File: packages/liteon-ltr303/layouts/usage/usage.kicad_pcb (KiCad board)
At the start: 2 copper layers, 5 parts

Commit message: fix checksum
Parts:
- R2, R3: value 10kΩ ±1% 62.5mW -> 4.7kΩ ±1% 62.5mW; footprint UNI_ROYAL_0402WGF1002TCE:R0402 -> UNI_ROYAL_0402WGF4701TCE:R0402
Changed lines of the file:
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@@
             )
         )
-        (property "checksum" "51bbabab493bf5d6f2e8ff7587227a5311f24aee7123d9f581721a4bd211b3f4"
+        (property "checksum" "ab8092c5206f4459d5858c652ec7d6e0be05596abb3bee276846f4a8302a4aa7"
             (at 0 0 0)
             (layer "User.9")
@@
             )
         )
-        (property "__atopile_lib_fp_hash__" "f4224e4a-fd5d-eb39-1573-fab7e7d24610"
+        (property "__atopile_lib_fp_hash__" "30b3a641-de78-5481-970c-0779282f0079"
             (at 0 0 0)
             (layer "User.9")
@@
         )
     )
-    (footprint "UNI_ROYAL_0402WGF1002TCE:R0402"
+    (footprint "UNI_ROYAL_0402WGF4701TCE:R0402"
         (layer "F.Cu")
         (at 0 -30 0)
@@
             )
         )
-        (property "Value" "10kΩ ±1% 62.5mW"
+        (property "Value" "4.7kΩ ±1% 62.5mW"
             (at 0 4 0)
             (layer "F.Fab")
@@
             )
         )
-        (property "checksum" "51bbabab493bf5d6f2e8ff7587227a5311f24aee7123d9f581721a4bd211b3f4"
+        (property "checksum" "0d598954a8da2c09676a6e60c961071badf97dacbdec513c849e6b4b9da6a890"
             (at 0 0 0)
             (layer "User.9")
@@
             )
         )
-        (property "__atopile_lib_fp_hash__" "f4224e4a-fd5d-eb39-1573-fab7e7d24610"
-            (at 0 0 0)
-            (layer "User.9")
-            (hide yes)
-            (effects
-                (font
-                    (size 0.125 0.125)
-                    (thickness 0.01875)
-                )
-            )
-        )
-        (property "LCSC" "C25744"
+        (property "__atopile_lib_fp_hash__" "78e51c6c-4851-23a9-a200-a953cf32da8a"
+            (at 0 0 0)
+            (layer "User.9")
+            (hide yes)
+            (effects
+                (font
+                    (size 0.125 0.125)
+                    (thickness 0.01875)
+                )
+            )
+        )
+        (property "LCSC" "C25900"
             (at 0 0 0)
             (layer "User.9")
@@
             )
         )
-        (property "Partnumber" "0402WGF1002TCE"
+        (property "Partnumber" "0402WGF4701TCE"
             (at 0 0 0)
             (layer "User.9")
@@
             )
         )
-        (property "PARAM_resistance" "{\"type\": \"Quantity_Interval_Disjoint\", \"data\": {\"intervals\": {\"type\": \"Numeric_Interval_Disjoint\", \"data\": {\"intervals\": [{\"type\": \"Numeric_Interval\", \"data\": {\"min\": 9900.000002235174, \"max\": 10099.999997764826}}]}}, \"unit\": \"ohm\"}}"
-            (at 0 0 0)
-            (layer "User.9")
-            (hide yes)
-            (effects
-                (font
-                    (size 0.125 0.125)
-                    (thickness 0.01875)
-                )
-            )
-        )
-        (property "Datasheet" "https://www.lcsc.com/datasheet/lcsc_datasheet_2411221126_UNI-ROYAL-Uniroyal-Elec-0402WGF1002TCE_C25744.pdf"
+        (property "PARAM_resistance" "{\"type\": \"Quantity_Interval_Disjoint\", \"data\": {\"intervals\": {\"type\": \"Numeric_Interval_Disjoint\", \"data\": {\"intervals\": [{\"type\": \"Numeric_Interval\", \"data\": {\"min\": 4653.000001050532, \"max\": 4746.999998949468}}]}}, \"unit\": \"ohm\"}}"
+            (at 0 0 0)
+            (layer "User.9")
+            (hide yes)
+            (effects
+                (font
+                    (size 0.125 0.125)
+                    (thickness 0.01875)
+                )
+            )
+        )
+        (property "Datasheet" "https://www.lcsc.com/datasheet/lcsc_datasheet_2206010045_UNI-ROYAL-Uniroyal-Elec-0402WGF4701TCE_C25900.pdf"
             (at 0 0 0)
             (layer "User.9")
@@
             (net 12 "SCL")
         )
-        (model "${KIPRJMOD}/../../parts/UNI_ROYAL_0402WGF1002TCE/R0402_L1.0-W0.5-H0.4.step"
+        (model "${KIPRJMOD}/../../parts/UNI_ROYAL_0402WGF4701TCE/R0402_L1.0-W0.5-H0.4.step"
             (offset
                 (xyz 0 0 0)
@@
         )
     )
-    (footprint "UNI_ROYAL_0402WGF1002TCE:R0402"
+    (footprint "UNI_ROYAL_0402WGF4701TCE:R0402"
         (layer "F.Cu")
         (at 0 -40 0)
@@
             )
         )
-        (property "Value" "10kΩ ±1% 62.5mW"
+        (property "Value" "4.7kΩ ±1% 62.5mW"
             (at 0 4 0)
             (layer "F.Fab")
@@
             )
         )
-        (property "checksum" "51bbabab493bf5d6f2e8ff7587227a5311f24aee7123d9f581721a4bd211b3f4"
+        (property "checksum" "0d598954a8da2c09676a6e60c961071badf97dacbdec513c849e6b4b9da6a890"
             (at 0 0 0)
             (layer "User.9")
@@
             )
         )
-        (property "__atopile_lib_fp_hash__" "f4224e4a-fd5d-eb39-1573-fab7e7d24610"
-            (at 0 0 0)
-            (layer "User.9")
-            (hide yes)
-            (effects
-                (font
-                    (size 0.125 0.125)
-                    (thickness 0.01875)
-                )
-            )
-        )
-        (property "LCSC" "C25744"
+        (property "__atopile_lib_fp_hash__" "78e51c6c-4851-23a9-a200-a953cf32da8a"
+            (at 0 0 0)
+            (layer "User.9")
+            (hide yes)
+            (effects
+                (font
+                    (size 0.125 0.125)
+                    (thickness 0.01875)
+                )
+            )
+        )
+        (property "LCSC" "C25900"
             (at 0 0 0)
             (layer "User.9")
@@
             )
         )
-        (property "Partnumber" "0402WGF1002TCE"
+        (property "Partnumber" "0402WGF4701TCE"
             (at 0 0 0)
             (layer "User.9")
@@
             )
         )
-        (property "PARAM_resistance" "{\"type\": \"Quantity_Interval_Disjoint\", \"data\": {\"intervals\": {\"type\": \"Numeric_Interval_Disjoint\", \"data\": {\"intervals\": [{\"type\": \"Numeric_Interval\", \"data\": {\"min\": 9900.000002235174, \"max\": 10099.999997764826}}]}}, \"unit\": \"ohm\"}}"
-            (at 0 0 0)
-            (layer "User.9")
-            (hide yes)
-            (effects
-                (font
-                    (size 0.125 0.125)
-                    (thickness 0.01875)
-                )
-            )
-        )
-        (property "Datasheet" "https://www.lcsc.com/datasheet/lcsc_datasheet_2411221126_UNI-ROYAL-Uniroyal-Elec-0402WGF1002TCE_C25744.pdf"
+        (property "PARAM_resistance" "{\"type\": \"Quantity_Interval_Disjoint\", \"data\": {\"intervals\": {\"type\": \"Numeric_Interval_Disjoint\", \"data\": {\"intervals\": [{\"type\": \"Numeric_Interval\", \"data\": {\"min\": 4653.000001050532, \"max\": 4746.999998949468}}]}}, \"unit\": \"ohm\"}}"
+            (at 0 0 0)
+            (layer "User.9")
+            (hide yes)
+            (effects
+                (font
+                    (size 0.125 0.125)
+                    (thickness 0.01875)
+                )
+            )
+        )
+        (property "Datasheet" "https://www.lcsc.com/datasheet/lcsc_datasheet_2206010045_UNI-ROYAL-Uniroyal-Elec-0402WGF4701TCE_C25900.pdf"
             (at 0 0 0)
             (layer "User.9")
@@
             (net 7 "SDA")
         )
-        (model "${KIPRJMOD}/../../parts/UNI_ROYAL_0402WGF1002TCE/R0402_L1.0-W0.5-H0.4.step"
+        (model "${KIPRJMOD}/../../parts/UNI_ROYAL_0402WGF4701TCE/R0402_L1.0-W0.5-H0.4.step"
             (offset
                 (xyz 0 0 0)

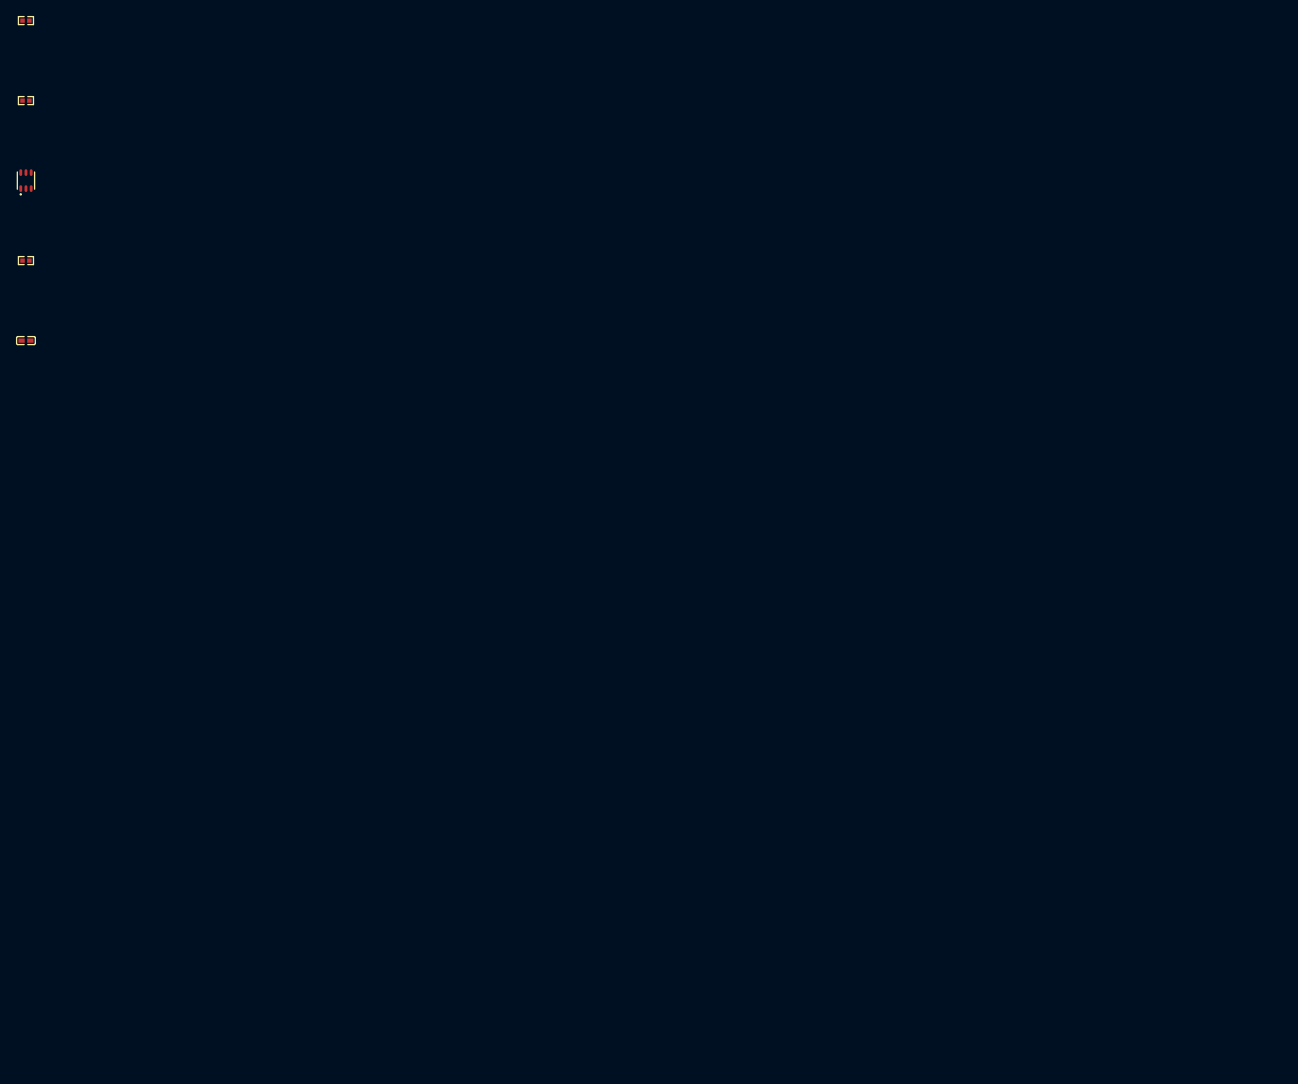
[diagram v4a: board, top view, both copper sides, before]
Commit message: fix layout liteon-ltr303
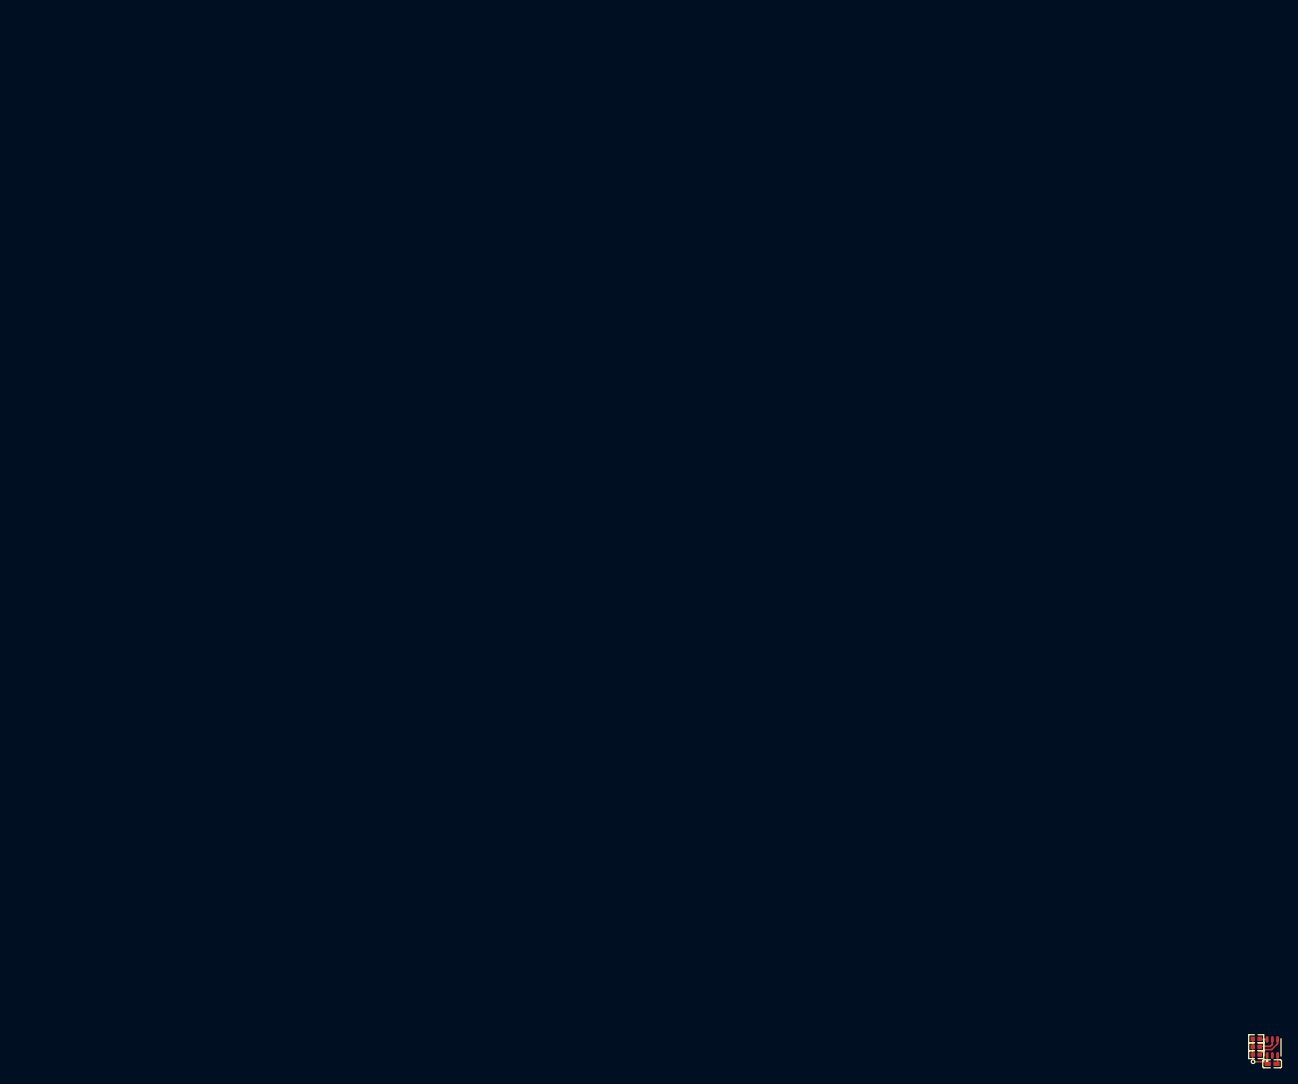
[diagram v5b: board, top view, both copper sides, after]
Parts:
- moved R3 199.6 mm to (153.8, 87.3), turned to 180 degrees
- moved R2 194.6 mm to (153.8, 89.2), turned to 180 degrees
- moved U1 189.8 mm to (155.8, 88.3)
- moved R1 182.5 mm to (153.8, 88.3), turned to 180 degrees
- moved C1 180.1 mm to (155.8, 90.4)
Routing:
- net hv: track 0.00 -> 5.90 mm, vias 0 -> 1
- net SCL: track 0.00 -> 3.34 mm
- net INT: track 0.00 -> 2.34 mm
- net gnd: track 0.00 -> 1.10 mm
- net SDA: track 0.00 -> 0.97 mm
